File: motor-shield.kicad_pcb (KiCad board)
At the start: 4 copper layers, 65.9 x 52.9 mm, 119 parts, among them J101 MC 1,5/ 2-G-3,5, J102 -, J103 MC 1,5/ 2-G-3,5, J104 -, J105 STEMMA QT, J106 Conn_02x04_smd, J107 Conn_01x04_f, J201 -, J202 -, J203 Barrel_Jack_MountingPin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

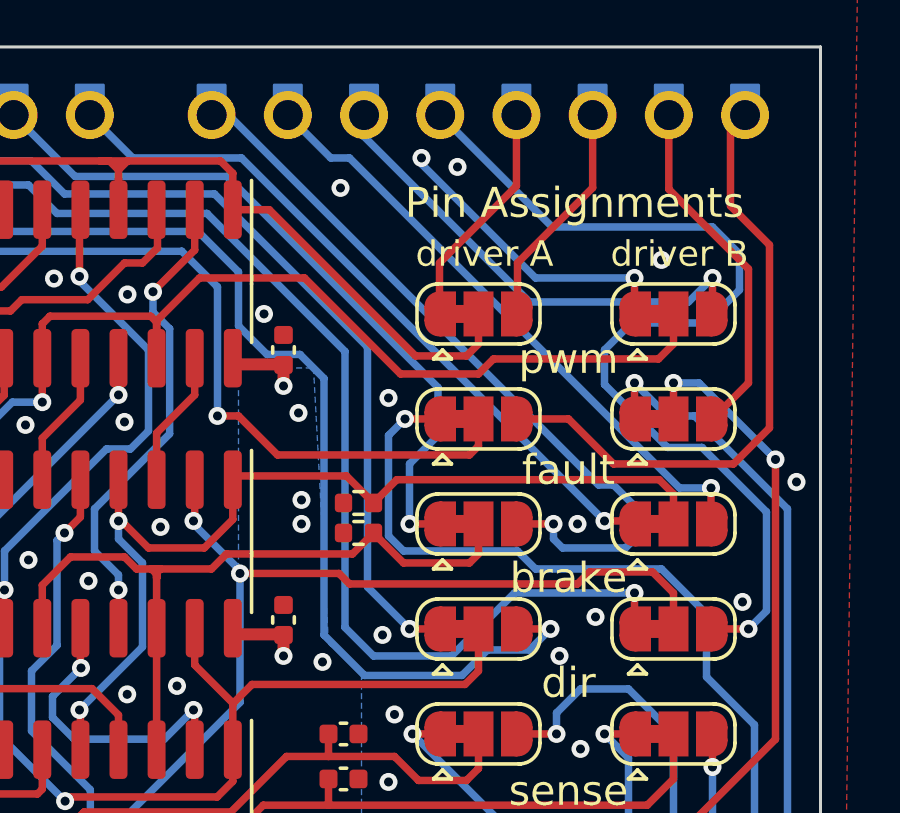
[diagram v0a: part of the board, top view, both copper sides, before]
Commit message: Add pulldowns and make all pulldowns larger
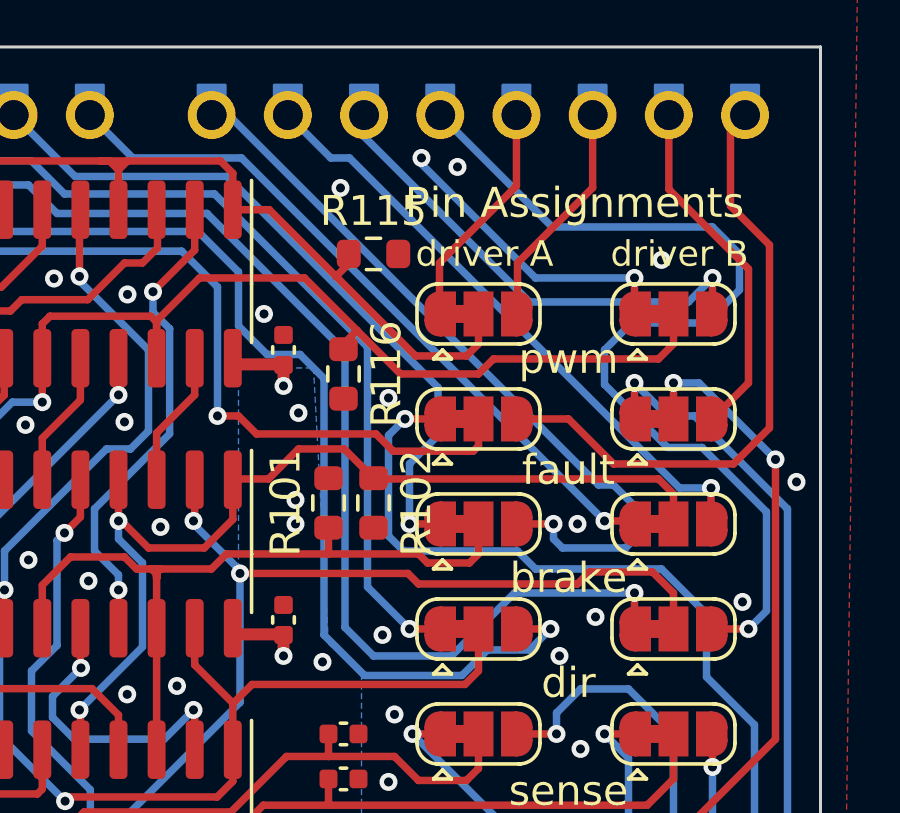
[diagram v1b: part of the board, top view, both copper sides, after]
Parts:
- added R115: 47k, Resistor_SMD:R_0603_1608Metric, F.Cu at (115.0, 65.5)
- added R116: 47k, Resistor_SMD:R_0603_1608Metric, F.Cu at (114.0, 69.5)
- R101, R102: footprint _my:R_1005_(0402) -> Resistor_SMD:R_0603_1608Metric
- moved R101 1.41 mm to (113.5, 73.8), turned to 90 degrees
- moved R102 0.50 mm to (115.0, 73.8), turned to -90 degrees
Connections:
- J201 pad 2: GND -> /Power/v_conn
- J203 pad MP: GND -> unconnected-(J203-MountPin-PadMP)
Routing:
- net /pwm_a: track 45.1 -> 46.1 mm
- net /pwm_b: track 56.8 -> 57.6 mm

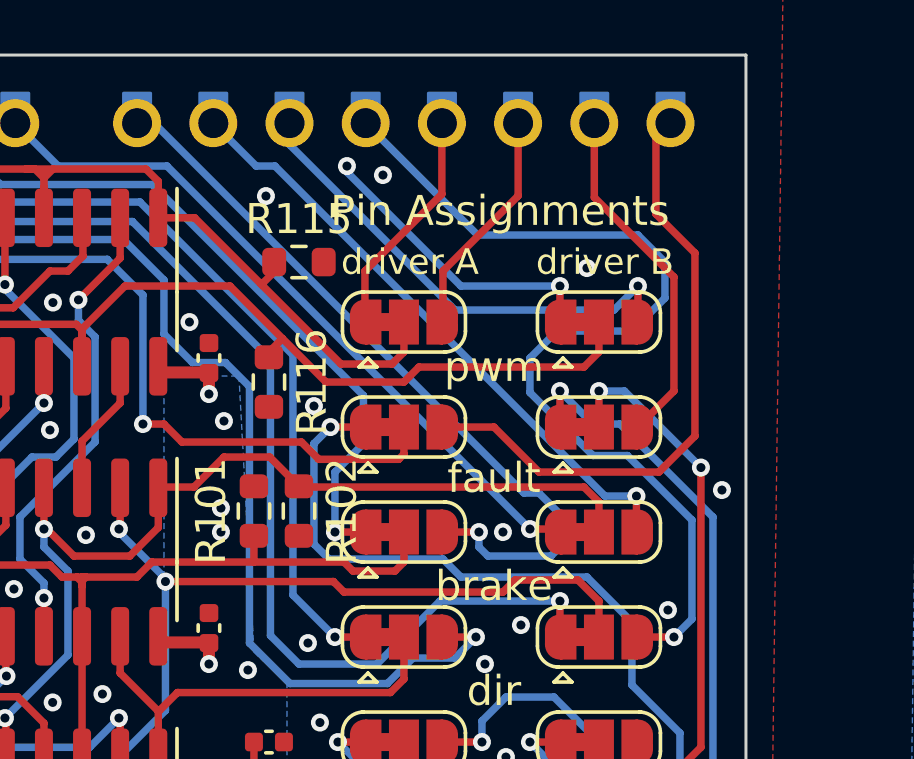
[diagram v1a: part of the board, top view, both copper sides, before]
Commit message: Move new resistor silkscreen out of the way
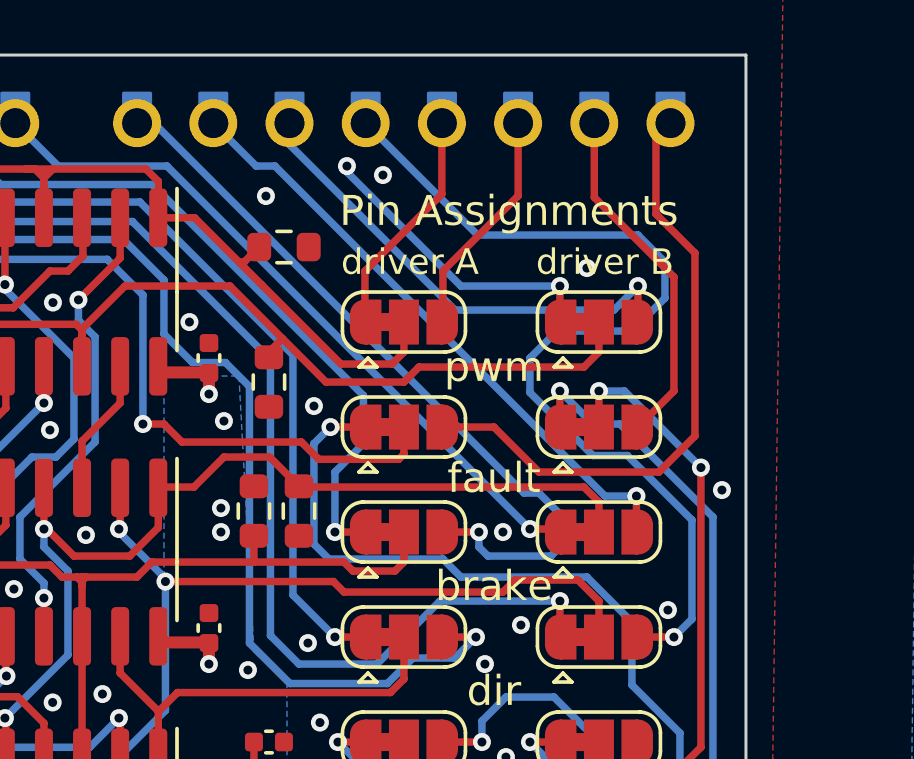
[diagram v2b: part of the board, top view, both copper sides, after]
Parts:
- moved R115 0.71 mm to (114.5, 65.0)
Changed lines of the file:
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@@
     (property "rohs_cert_or_in_datasheet" "y")
     (attr smd)
-    (fp_text reference "R101" (at 0 -1.43 90) (layer "F.SilkS")
+    (fp_text reference "R101" (at 0 -1.43 90) (layer "F.SilkS") hide
         (effects (font (size 1 1) (thickness 0.15)))
     )
@@
     (property "rohs_cert_or_in_datasheet" "y")
     (attr smd)
-    (fp_text reference "R116" (at 0 -1.43 90) (layer "F.SilkS")
+    (fp_text reference "R116" (at 0 -1.43 90) (layer "F.SilkS") hide
         (effects (font (size 1 1) (thickness 0.15)))
     )
@@
     (property "rohs_cert_or_in_datasheet" "y")
     (attr smd)
-    (fp_text reference "R102" (at 0 -1.43 90) (layer "F.SilkS")
+    (fp_text reference "R102" (at 0 -1.43 90) (layer "F.SilkS") hide
         (effects (font (size 1 1) (thickness 0.15)))
     )
@@
   )
   (footprint "Resistor_SMD:R_0603_1608Metric" (layer "F.Cu")
-    (at 115 65.5)
+    (at 114.5 65)
     (descr "Resistor SMD 0603 (1608 Metric), square (rectangular) end terminal, IPC_7351 nominal, (Body size source: IPC-SM-782 page 72, https://www.pcb-3d.com/wordpress/wp-content/uploads/ipc-sm-782a_amendment_1_and_2.pdf), generated with kicad-footprint-generator")
     (tags "resistor")
@@
     (property "rohs_cert_or_in_datasheet" "y")
     (attr smd)
-    (fp_text reference "R115" (at 0 -1.43) (layer "F.SilkS")
+    (fp_text reference "R115" (at 0 -1.43) (layer "F.SilkS") hide
         (effects (font (size 1 1) (thickness 0.15)))
     )
@@
     (effects (font (size 0.85 0.85) (thickness 0.15)) (justify left))
   )
-  (gr_text "Pin Assignments" (at 121.7 63.8) (layer "F.SilkS")
+  (gr_text "Pin Assignments" (at 122 63.8) (layer "F.SilkS")
     (effects (font (size 1 1) (thickness 0.17)))
   )
@@
   (segment (start 111.525 64.025) (end 110.31 64.025) (width 0.25) (layer "F.Cu") (net 18))
   (segment (start 96.2 76) (end 95 76) (width 0.25) (layer "F.Cu") (net 18))
-  (segment (start 114.175 65.5) (end 114.175 65.825) (width 0.25) (layer "F.Cu") (net 18))
+  (segment (start 113.175 65.5) (end 113.675 65) (width 0.25) (layer "F.Cu") (net 18))
   (segment (start 118.5 68.5) (end 118.1 68.9) (width 0.25) (layer "F.Cu") (net 18))
   (segment (start 106.2 62.4) (end 105.9 62.4) (width 0.25) (layer "F.Cu") (net 18))
@@
   (segment (start 97.025 65.475) (end 96.2 66.3) (width 0.25) (layer "F.Cu") (net 18))
   (segment (start 106.5 63) (end 106.5 62.7) (width 0.25) (layer "F.Cu") (net 18))
-  (segment (start 113.75 66.25) (end 111.525 64.025) (width 0.25) (layer "F.Cu") (net 18))
+  (segment (start 113 65.5) (end 113.175 65.5) (width 0.25) (layer "F.Cu") (net 18))
   (segment (start 106.8 62.4) (end 109.9 62.4) (width 0.25) (layer "F.Cu") (net 18))
+  (segment (start 113 65.5) (end 111.525 64.025) (width 0.25) (layer "F.Cu") (net 18))
   (segment (start 105.9 62.4) (end 101.6 62.4) (width 0.25) (layer "F.Cu") (net 18))
+  (segment (start 113.75 66.25) (end 113 65.5) (width 0.25) (layer "F.Cu") (net 18))
   (segment (start 118.5 67.5) (end 118.5 68.5) (width 0.25) (layer "F.Cu") (net 18))
   (segment (start 106.5 62.7) (end 106.8 62.4) (width 0.25) (layer "F.Cu") (net 18))
   (segment (start 109.9 62.4) (end 110.31 62.81) (width 0.25) (layer "F.Cu") (net 18))
   (segment (start 106.5 64.025) (end 106.5 63) (width 0.25) (layer "F.Cu") (net 18))
-  (segment (start 114.175 65.825) (end 113.75 66.25) (width 0.25) (layer "F.Cu") (net 18))
   (segment (start 97.025 65.475) (end 98.525 65.475) (width 0.25) (layer "F.Cu") (net 18))
   (segment (start 110.31 62.81) (end 110.31 64.025) (width 0.25) (layer "F.Cu") (net 18))
